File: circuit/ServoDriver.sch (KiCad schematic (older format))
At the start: 9 parts, among them U1 STM32F042K6Tx

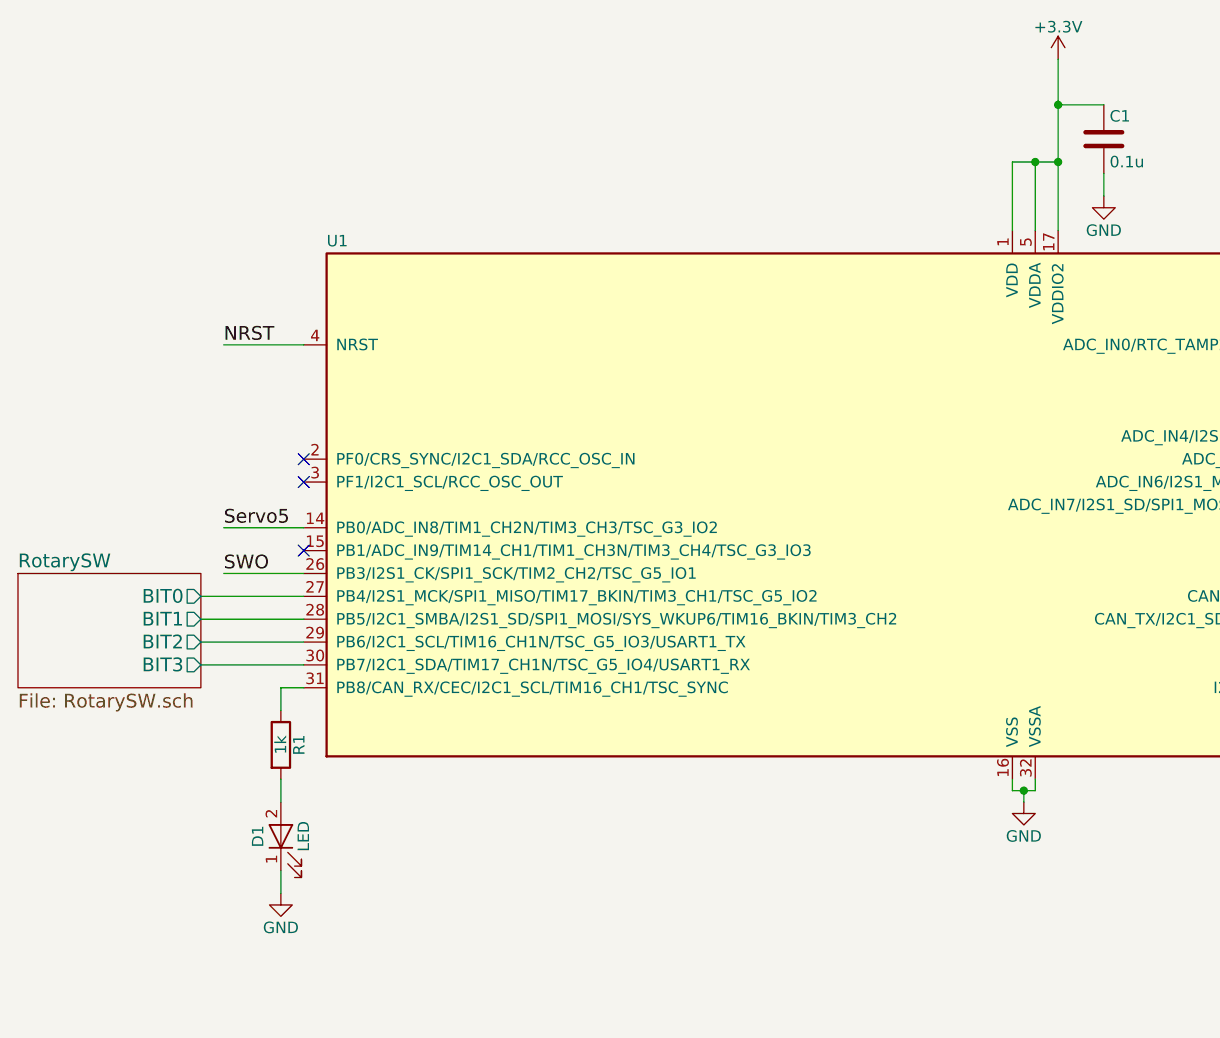
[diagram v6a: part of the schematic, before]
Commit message: ロータリースイッチとLEDのピンを変更
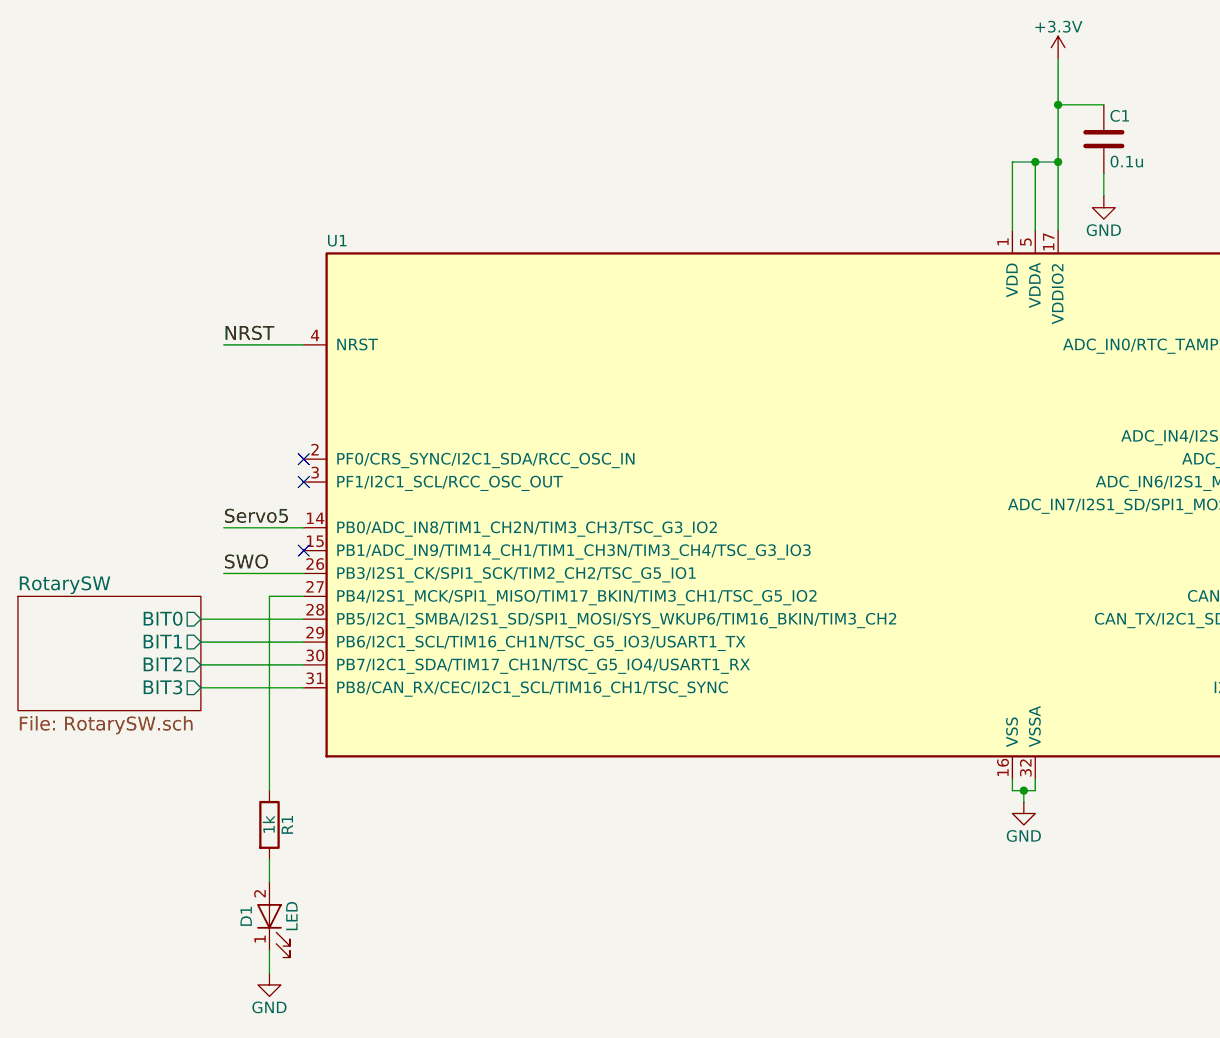
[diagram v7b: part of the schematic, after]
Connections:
- net RotarySW/BIT0: now also U1.28 (PB5/I2C1_SMBA/I2S1_SD/SPI1_MOSI/SYS_WKUP6/TIM16_BKIN/TIM3_CH2); no longer U1.27 (PB4/I2S1_MCK/SPI1_MISO/TIM17_BKIN/TIM3_CH1/TSC_G5_IO2)
- net RotarySW/BIT1: now also U1.29 (PB6/I2C1_SCL/TIM16_CH1N/TSC_G5_IO3/USART1_TX); no longer U1.28 (PB5/I2C1_SMBA/I2S1_SD/SPI1_MOSI/SYS_WKUP6/TIM16_BKIN/TIM3_CH2)
- net RotarySW/BIT2: now also U1.30 (PB7/I2C1_SDA/TIM17_CH1N/TSC_G5_IO4/USART1_RX); no longer U1.29 (PB6/I2C1_SCL/TIM16_CH1N/TSC_G5_IO3/USART1_TX)
- net RotarySW/BIT3: now also U1.31 (PB8/CAN_RX/CEC/I2C1_SCL/TIM16_CH1/TSC_SYNC); no longer U1.30 (PB7/I2C1_SDA/TIM17_CH1N/TSC_G5_IO4/USART1_RX)
- net at R1.1: now also U1.27 (PB4/I2S1_MCK/SPI1_MISO/TIM17_BKIN/TIM3_CH1/TSC_G5_IO2); no longer U1.31 (PB8/CAN_RX/CEC/I2C1_SCL/TIM16_CH1/TSC_SYNC)
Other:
- moved on the sheet: D1, R1
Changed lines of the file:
@@
 LIBS:valves
 LIBS:stm32
+LIBS:robocon_sch
+LIBS:SamacSys_Parts
+LIBS:YASU
 LIBS:ServoDriver-cache
 EELAYER 25 0
@@
 Servo0
 $Sheet
-S 600  4750 800  500
+S 600  4850 800  500
 U 594B68C0
 F0 "RotarySW" 60
 F1 "RotarySW.sch" 60
-F2 "BIT0" O R 1400 4850 60
-F3 "BIT1" O R 1400 4950 60
-F4 "BIT2" O R 1400 5050 60
-F5 "BIT3" O R 1400 5150 60
+F2 "BIT0" O R 1400 4950 60
+F3 "BIT1" O R 1400 5050 60
+F4 "BIT2" O R 1400 5150 60
+F5 "BIT3" O R 1400 5250 60
 $EndSheet
 NoConn ~ 1850 4250
@@
 L R R1
 U 1 1 5972773B
-P 1750 5500
-F 0 "R1" V 1830 5500 50  0000 C CNN
-F 1 "1k" V 1750 5500 50  0000 C CNN
-F 2 "Resistors_SMD:R_0603_HandSoldering" V 1680 5500 50  0001 C CNN
-F 3 "" H 1750 5500 50  0001 C CNN
-	1    1750 5500
+P 1700 5850
+F 0 "R1" V 1780 5850 50  0000 C CNN
+F 1 "1k" V 1700 5850 50  0000 C CNN
+F 2 "Resistors_SMD:R_0603_HandSoldering" V 1630 5850 50  0001 C CNN
+F 3 "" H 1700 5850 50  0001 C CNN
+	1    1700 5850
 	1    0    0    -1
 $EndComp
@@
 L LED D1
 U 1 1 59727C65
-P 1750 5900
-F 0 "D1" H 1750 6000 50  0000 C CNN
-F 1 "LED" H 1750 5800 50  0000 C CNN
-F 2 "LEDs:LED_D5.0mm" H 1750 5900 50  0001 C CNN
-F 3 "" H 1750 5900 50  0001 C CNN
-	1    1750 5900
+P 1700 6250
+F 0 "D1" H 1700 6350 50  0000 C CNN
+F 1 "LED" H 1700 6150 50  0000 C CNN
+F 2 "LEDs:LED_D5.0mm" H 1700 6250 50  0001 C CNN
+F 3 "" H 1700 6250 50  0001 C CNN
+	1    1700 6250
 	0    -1   -1   0
 $EndComp
@@
 L GND #PWR08
 U 1 1 59728230
-P 1750 6150
-F 0 "#PWR08" H 1750 5900 50  0001 C CNN
-F 1 "GND" H 1750 6000 50  0000 C CNN
-F 2 "" H 1750 6150 50  0001 C CNN
-F 3 "" H 1750 6150 50  0001 C CNN
-	1    1750 6150
+P 1700 6500
+F 0 "#PWR08" H 1700 6250 50  0001 C CNN
+F 1 "GND" H 1700 6350 50  0000 C CNN
+F 2 "" H 1700 6500 50  0001 C CNN
+F 3 "" H 1700 6500 50  0001 C CNN
+	1    1700 6500
 	1    0    0    -1
 $EndComp
@@
 	4950 3250 4950 2950
 Wire Wire Line
-	4950 2950 5150 2950
+	5150 2950 4950 2950
 Wire Wire Line
 	5150 2500 5150 3250
@@
 	8250 5150 8600 5150
 Wire Wire Line
-	1400 4850 1850 4850
-Wire Wire Line
-	1850 4950 1400 4950
-Wire Wire Line
-	1400 5050 1850 5050
-Wire Wire Line
-	1850 5150 1400 5150
+	1400 4950 1850 4950
+Wire Wire Line
+	1850 5050 1400 5050
+Wire Wire Line
+	1400 5150 1850 5150
+Wire Wire Line
+	1850 5250 1400 5250
 Wire Wire Line
 	10100 1900 10100 1750
@@
 	8650 4150 8950 4150
 Wire Wire Line
-	1750 5350 1750 5250
-Wire Wire Line
-	1750 5250 1850 5250
-Wire Wire Line
-	1750 5650 1750 5750
-Wire Wire Line
-	1750 6050 1750 6150
+	1700 4850 1850 4850
+Wire Wire Line
+	1700 6000 1700 6100
+Wire Wire Line
+	1700 6400 1700 6500
 Wire Wire Line
 	8350 5650 8350 5750
@@
 Wire Wire Line
 	1500 4550 1850 4550
+Wire Wire Line
+	1700 4850 1700 5700
 $EndSCHEMATC

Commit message: ロータリースイッチの配線終わり
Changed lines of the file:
@@
 	4950 3250 4950 2950
 Wire Wire Line
-	5150 2950 4950 2950
+	4950 2950 5150 2950
 Wire Wire Line
 	5150 2500 5150 3250
